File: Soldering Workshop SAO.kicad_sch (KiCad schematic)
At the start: 11 parts, among them J1 Conn_02x03_Odd_Even, SW1 SW_SPDT, U1 LMC555xM

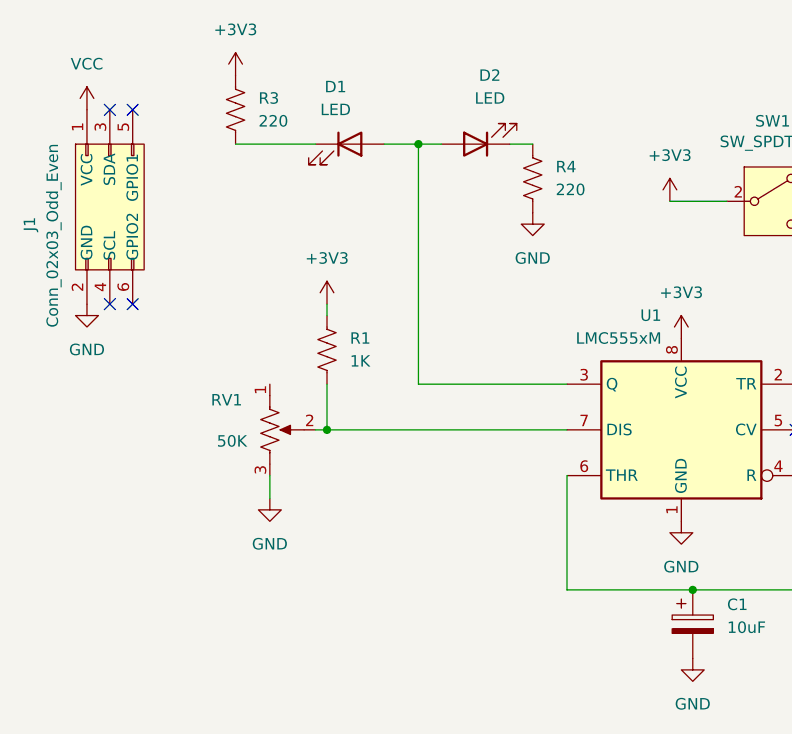
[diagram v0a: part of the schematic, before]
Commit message: Revision B
do not blindly trust schematics you find on the internet

Connect Th to Tr
Disconnect RV1 from GND
Connect RV1 to Th
Flip D1
Put D1 on silk
put MAGFEST on the schematic
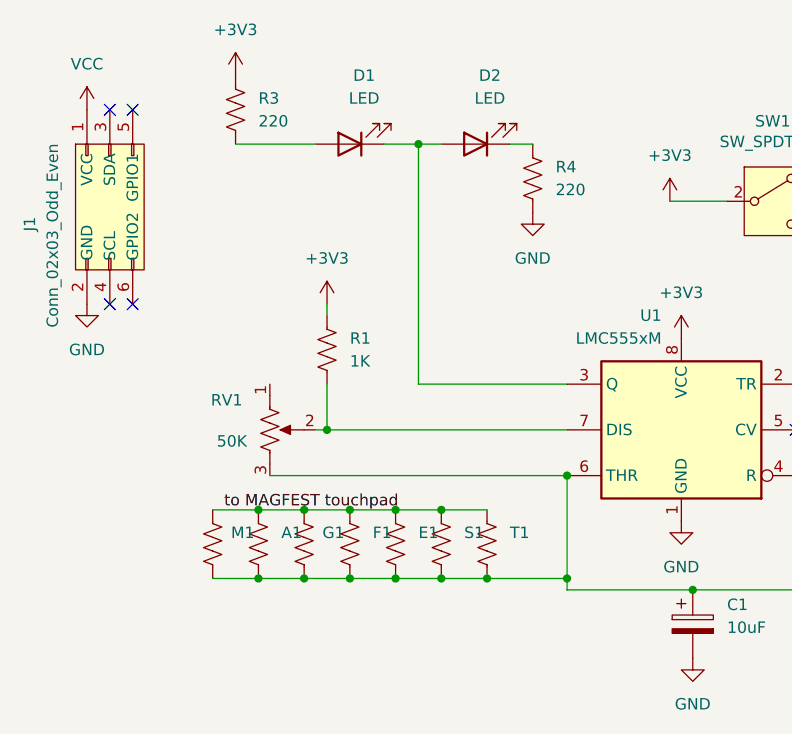
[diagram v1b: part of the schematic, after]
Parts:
- added A1, E1, F1, G1, M1, S1, T1: 220, Resistor_THT:R_Axial_DIN0204_L3.6mm_D1.6mm_P7.62mm_Horizontal, symbol Device:R_US
- BATTERY1: footprint CONN3_1775485-1_TEC -> sao:CONN3_1775485-1_TEC
- RV1: footprint sao:RK10J11E0034 -> sao:91AR50KLF
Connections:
- net GND: no longer RV1.3
- net at D1.1 (K): now also D2.2 (A), U1.3 (Q); no longer R3.1
- net at C1.1, U1.2 (TR), U1.6 (THR): now also RV1.3, A1.1, E1.1, F1.1, G1.1, M1.1, S1.1, T1.1
- new net: D1.2 (A), R3.1
- new net to MAGFEST touchpad: A1.2, E1.2, F1.2, G1.2, M1.2, S1.2, T1.2
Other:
- moved on the sheet: D1

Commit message: cleanup data, readme
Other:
- company: (none) -> MAGFEST INC
- title: (none) -> 2025 MAGFEST SOLDERING WORKSHOP
- moved on the sheet: A1, BATTERY1, C1, D1, D2, E1, F1, G1, J1, M1, R1, R3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
